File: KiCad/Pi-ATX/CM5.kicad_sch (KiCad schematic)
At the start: 1 part

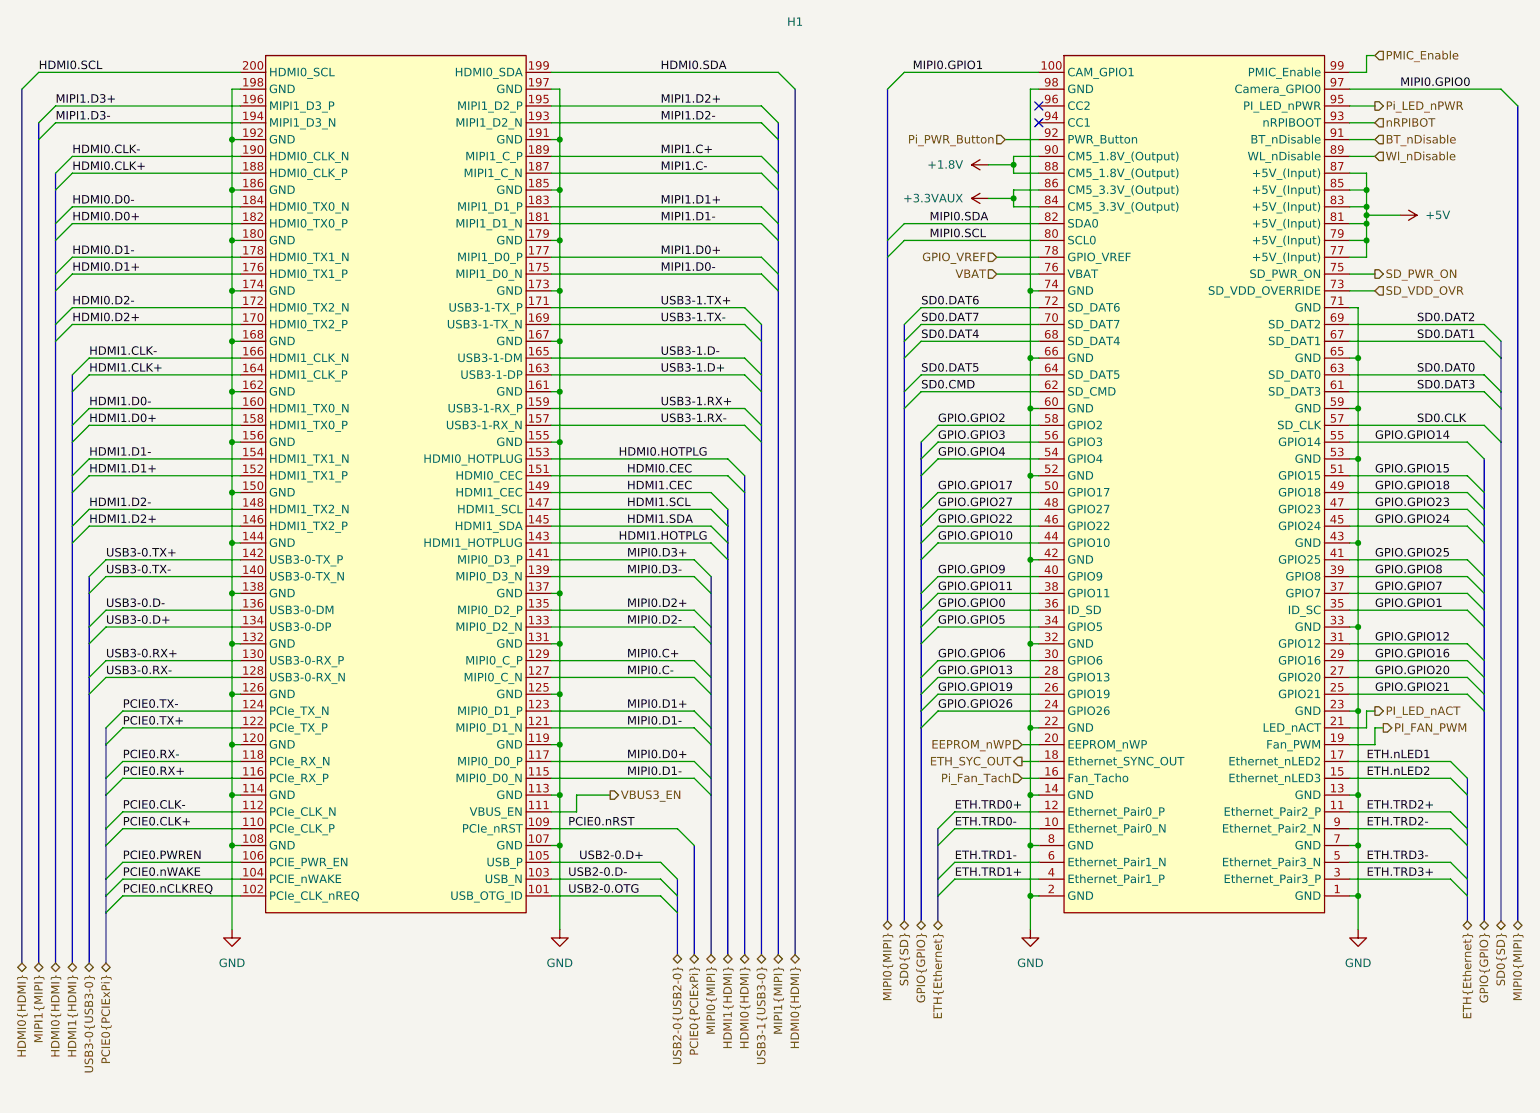
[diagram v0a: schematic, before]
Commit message: Finished MIPI Connector Schematic
-finished MIPI connector schematic page
-updated CM5 symbol to v0.2 version from my RPI CM library
-updated to do list
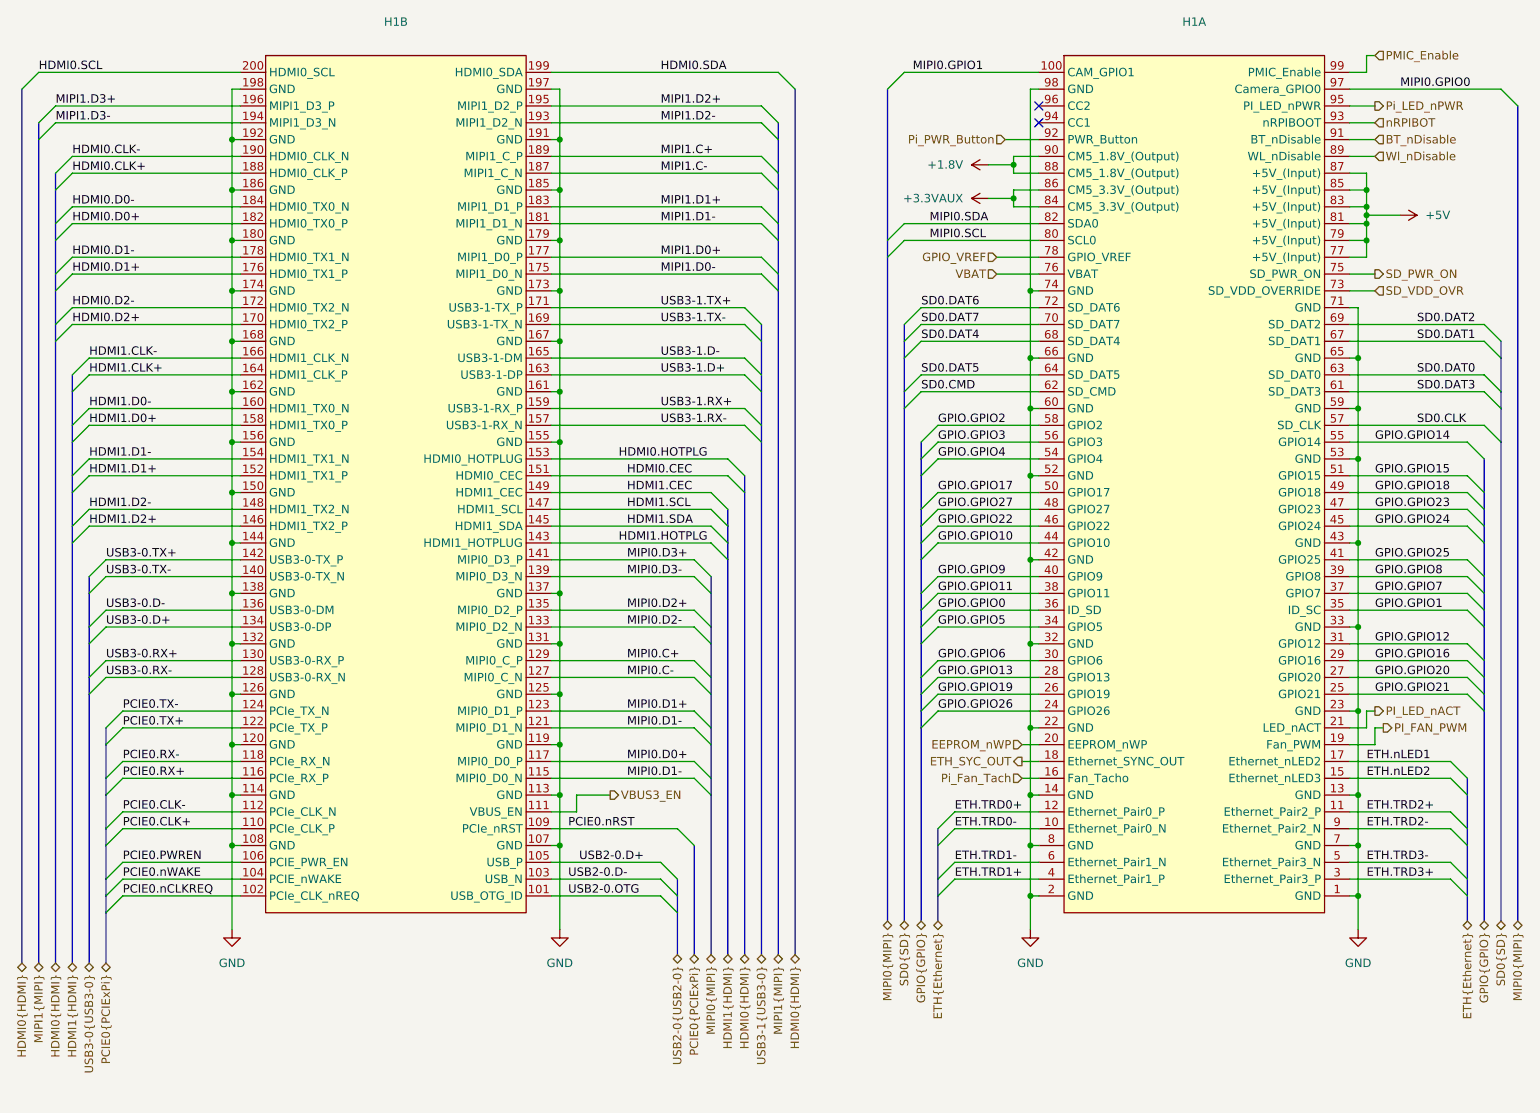
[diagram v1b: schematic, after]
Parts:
- added unit 2 of H1
- H1: Note Use connector 10164227-1001A1RLF for short stackup hieght. 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 -> (none)
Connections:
- net GND: now also H1.107 (GND), H1.108 (GND), H1.113 (GND), H1.114 (GND), H1.119 (GND), H1.120 (GND), H1.125 (GND), H1.126 (GND), H1.131 (GND), H1.132 (GND), H1.137 (GND), H1.138 (GND), H1.144 (GND), H1.150 (GND), H1.155 (GND), H1.156 (GND), H1.161 (GND), H1.162 (GND), H1.167 (GND), H1.168 (GND), H1.173 (GND), H1.174 (GND), H1.179 (GND), H1.180 (GND), H1.185 (GND), H1.186 (GND), H1.191 (GND), H1.192 (GND), H1.197 (GND), H1.198 (GND); no longer H1.107 (GND), H1.108 (GND), H1.113 (GND), H1.114 (GND), H1.119 (GND), H1.120 (GND), H1.125 (GND), H1.126 (GND), H1.131 (GND), H1.132 (GND), H1.137 (GND), H1.138 (GND), H1.144 (GND), H1.150 (GND), H1.155 (GND), H1.156 (GND), H1.161 (GND), H1.162 (GND), H1.167 (GND), H1.168 (GND), H1.173 (GND), H1.174 (GND), H1.179 (GND), H1.180 (GND), H1.185 (GND), H1.186 (GND), H1.191 (GND), H1.192 (GND), H1.197 (GND), H1.198 (GND)
- net HDMI0.CEC: now also H1.151 (HDMI0_CEC); no longer H1.151 (HDMI0_CEC)
- net HDMI0.CLK+: now also H1.188 (HDMI0_CLK_P); no longer H1.188 (HDMI0_CLK_P)
- net HDMI0.CLK-: now also H1.190 (HDMI0_CLK_N); no longer H1.190 (HDMI0_CLK_N)
- net HDMI0.D0+: now also H1.182 (HDMI0_TX0_P); no longer H1.182 (HDMI0_TX0_P)
- net HDMI0.D0-: now also H1.184 (HDMI0_TX0_N); no longer H1.184 (HDMI0_TX0_N)
- net HDMI0.D1+: now also H1.176 (HDMI0_TX1_P); no longer H1.176 (HDMI0_TX1_P)
- net HDMI0.D1-: now also H1.178 (HDMI0_TX1_N); no longer H1.178 (HDMI0_TX1_N)
- net HDMI0.D2+: now also H1.170 (HDMI0_TX2_P); no longer H1.170 (HDMI0_TX2_P)
- net HDMI0.D2-: now also H1.172 (HDMI0_TX2_N); no longer H1.172 (HDMI0_TX2_N)
- net HDMI0.HOTPLG: now also H1.153 (HDMI0_HOTPLUG); no longer H1.153 (HDMI0_HOTPLUG)
- net HDMI0.SCL: now also H1.200 (HDMI0_SCL); no longer H1.200 (HDMI0_SCL)
- net HDMI0.SDA: now also H1.199 (HDMI0_SDA); no longer H1.199 (HDMI0_SDA)
- net HDMI1.CEC: now also H1.149 (HDMI1_CEC); no longer H1.149 (HDMI1_CEC)
- net HDMI1.CLK+: now also H1.164 (HDMI1_CLK_P); no longer H1.164 (HDMI1_CLK_P)
- net HDMI1.CLK-: now also H1.166 (HDMI1_CLK_N); no longer H1.166 (HDMI1_CLK_N)
- net HDMI1.D0+: now also H1.158 (HDMI1_TX0_P); no longer H1.158 (HDMI1_TX0_P)
- net HDMI1.D0-: now also H1.160 (HDMI1_TX0_N); no longer H1.160 (HDMI1_TX0_N)
- net HDMI1.D1+: now also H1.152 (HDMI1_TX1_P); no longer H1.152 (HDMI1_TX1_P)
- net HDMI1.D1-: now also H1.154 (HDMI1_TX1_N); no longer H1.154 (HDMI1_TX1_N)
- net HDMI1.D2+: now also H1.146 (HDMI1_TX2_P); no longer H1.146 (HDMI1_TX2_P)
- net HDMI1.D2-: now also H1.148 (HDMI1_TX2_N); no longer H1.148 (HDMI1_TX2_N)
- net HDMI1.HOTPLG: now also H1.143 (HDMI1_HOTPLUG); no longer H1.143 (HDMI1_HOTPLUG)
- net HDMI1.SCL: now also H1.147 (HDMI1_SCL); no longer H1.147 (HDMI1_SCL)
- net HDMI1.SDA: now also H1.145 (HDMI1_SDA); no longer H1.145 (HDMI1_SDA)
- net MIPI0.C+: now also H1.129 (MIPI0_C_P); no longer H1.129 (MIPI0_C_P)
- net MIPI0.C-: now also H1.127 (MIPI0_C_N); no longer H1.127 (MIPI0_C_N)
- net MIPI0.D0+: now also H1.117 (MIPI0_D0_P); no longer H1.117 (MIPI0_D0_P)
- net MIPI0.D1+: now also H1.123 (MIPI0_D1_P); no longer H1.123 (MIPI0_D1_P)
- net MIPI0.D1-: now also H1.115 (MIPI0_D0_N), H1.121 (MIPI0_D1_N); no longer H1.115 (MIPI0_D0_N), H1.121 (MIPI0_D1_N)
- net MIPI0.D2+: now also H1.135 (MIPI0_D2_P); no longer H1.135 (MIPI0_D2_P)
- net MIPI0.D2-: now also H1.133 (MIPI0_D2_N); no longer H1.133 (MIPI0_D2_N)
- net MIPI0.D3+: now also H1.141 (MIPI0_D3_P); no longer H1.141 (MIPI0_D3_P)
- net MIPI0.D3-: now also H1.139 (MIPI0_D3_N); no longer H1.139 (MIPI0_D3_N)
- net MIPI1.C+: now also H1.189 (MIPI1_C_P); no longer H1.189 (MIPI1_C_P)
- net MIPI1.C-: now also H1.187 (MIPI1_C_N); no longer H1.187 (MIPI1_C_N)
- net MIPI1.D0+: now also H1.177 (MIPI1_D0_P); no longer H1.177 (MIPI1_D0_P)
- net MIPI1.D0-: now also H1.175 (MIPI1_D0_N); no longer H1.175 (MIPI1_D0_N)
- net MIPI1.D1+: now also H1.183 (MIPI1_D1_P); no longer H1.183 (MIPI1_D1_P)
- net MIPI1.D1-: now also H1.181 (MIPI1_D1_N); no longer H1.181 (MIPI1_D1_N)
- net MIPI1.D2+: now also H1.195 (MIPI1_D2_P); no longer H1.195 (MIPI1_D2_P)
- net MIPI1.D2-: now also H1.193 (MIPI1_D2_N); no longer H1.193 (MIPI1_D2_N)
- net MIPI1.D3+: now also H1.196 (MIPI1_D3_P); no longer H1.196 (MIPI1_D3_P)
- net MIPI1.D3-: now also H1.194 (MIPI1_D3_N); no longer H1.194 (MIPI1_D3_N)
- net PCIE0.CLK+: now also H1.110 (PCIe_CLK_P); no longer H1.110 (PCIe_CLK_P)
- net PCIE0.CLK-: now also H1.112 (PCIe_CLK_N); no longer H1.112 (PCIe_CLK_N)
- net PCIE0.PWREN: now also H1.106 (PCIE_PWR_EN); no longer H1.106 (PCIE_PWR_EN)
- net PCIE0.RX+: now also H1.116 (PCIe_RX_P); no longer H1.116 (PCIe_RX_P)
- net PCIE0.RX-: now also H1.118 (PCIe_RX_N); no longer H1.118 (PCIe_RX_N)
- net PCIE0.TX+: now also H1.122 (PCIe_TX_P); no longer H1.122 (PCIe_TX_P)
- net PCIE0.TX-: now also H1.124 (PCIe_TX_N); no longer H1.124 (PCIe_TX_N)
- net PCIE0.nCLKREQ: now also H1.102 (PCIe_CLK_nREQ); no longer H1.102 (PCIe_CLK_nREQ)
- net PCIE0.nRST: now also H1.109 (PCIe_nRST); no longer H1.109 (PCIe_nRST)
- net PCIE0.nWAKE: now also H1.104 (PCIE_nWAKE); no longer H1.104 (PCIE_nWAKE)
- net USB2-0.D+: now also H1.105 (USB_P); no longer H1.105 (USB_P)
- net USB2-0.D-: now also H1.103 (USB_N); no longer H1.103 (USB_N)
- net USB2-0.OTG: now also H1.101 (USB_OTG_ID); no longer H1.101 (USB_OTG_ID)
- net USB3-0.D+: now also H1.134 (USB3-0-DP); no longer H1.134 (USB3-0-DP)
- net USB3-0.D-: now also H1.136 (USB3-0-DM); no longer H1.136 (USB3-0-DM)
- net USB3-0.RX+: now also H1.130 (USB3-0-RX_P); no longer H1.130 (USB3-0-RX_P)
- net USB3-0.RX-: now also H1.128 (USB3-0-RX_N); no longer H1.128 (USB3-0-RX_N)
- net USB3-0.TX+: now also H1.142 (USB3-0-TX_P); no longer H1.142 (USB3-0-TX_P)
- net USB3-0.TX-: now also H1.140 (USB3-0-TX_N); no longer H1.140 (USB3-0-TX_N)
- net USB3-1.D+: now also H1.163 (USB3-1-DP); no longer H1.163 (USB3-1-DP)
- net USB3-1.D-: now also H1.165 (USB3-1-DM); no longer H1.165 (USB3-1-DM)
- net USB3-1.RX+: now also H1.159 (USB3-1-RX_P); no longer H1.159 (USB3-1-RX_P)
- net USB3-1.RX-: now also H1.157 (USB3-1-RX_N); no longer H1.157 (USB3-1-RX_N)
- net USB3-1.TX+: now also H1.171 (USB3-1-TX_P); no longer H1.171 (USB3-1-TX_P)
- net USB3-1.TX-: now also H1.169 (USB3-1-TX_N); no longer H1.169 (USB3-1-TX_N)
- net VBUS3_EN: now also H1.111 (VBUS_EN); no longer H1.111 (VBUS_EN)
